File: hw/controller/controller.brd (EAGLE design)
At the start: 46 x 53 mm, 100 parts, among them J1 XT30XT30PW_MALE, J2 XT30XT30PW_MALE, M1 MOUNT, M2 MOUNT, M3 MOUNT, M4 MOUNT, Q1 TPH1R204PLSOP_ADVANCE_8, Q2 TPH1R204PLSOP_ADVANCE_8, Q3 TPH1R204PLSOP_ADVANCE_8, Q4 TPH1R204PLSOP_ADVANCE_8, Q5 TPH1R204PLSOP_ADVANCE_8, Q6 TPH1R204PLSOP_ADVANCE_8, U1 STM32G474CEU6, U2 TCAN334G, U3 AS5147, U4 DRV8323RS

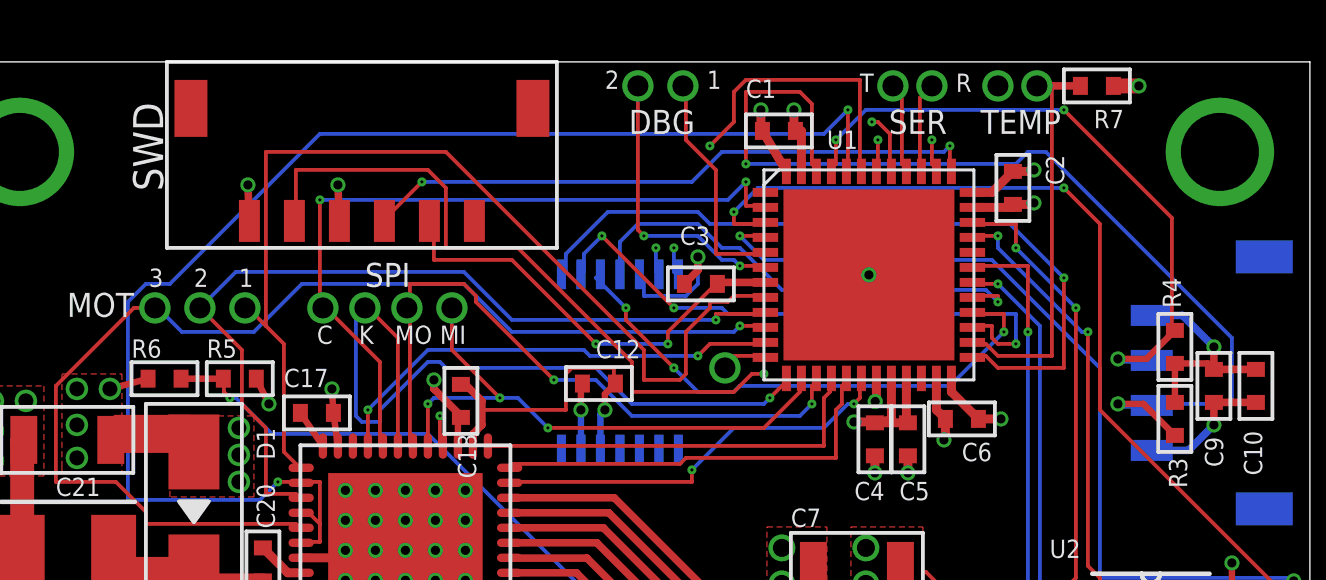
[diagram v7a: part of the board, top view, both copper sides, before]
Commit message: Add some more ground debug pins
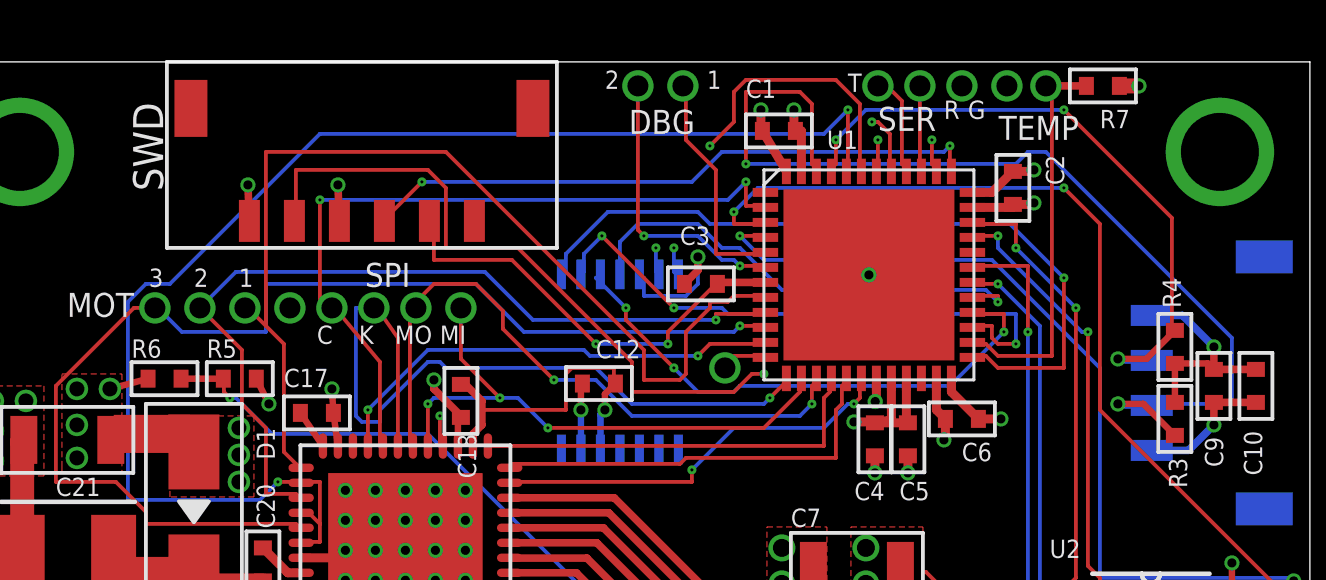
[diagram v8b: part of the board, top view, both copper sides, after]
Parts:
- added DG1, DG2: PAD24AWG_PAD, controller:24AWG_PAD
- moved DTX 0.50 mm to (8.60, 9.20)
- moved DTR 0.40 mm to (10.0, 9.20)
- moved DRV_CS 0.30 mm to (-9.60, 1.80)
- moved DRV_SCK 0.30 mm to (-8.20, 1.80)
- moved TEMP1 0.30 mm to (12.9, 9.20)
- moved DRV_MISO 0.30 mm to (-5.30, 1.80)
- moved DRV_MOSI 0.30 mm to (-6.80, 1.80)
- moved TEMP2 0.30 mm to (14.2, 9.20)
- moved R7 0.20 mm to (16.1, 9.20)
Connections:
- net GND: now also DG1.P$1, DG2.P$1
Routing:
- net MOTOR3: track 38.7 -> 39.7 mm
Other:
- board text added: "G"
